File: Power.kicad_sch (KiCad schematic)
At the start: 82 parts, among them Q1 WPM1481-6/TR, U1 H3, U2 AXP223_C2997893

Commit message: linking symbols to footprints
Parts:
- C1, C10, C13, C14, C2, C27, C29, C3, C30, C31, C32, C33, C34, C36, C4, C41, C42, C43, C44, C45, C46, C47, C48, C49, C50, C53, C54, C55, C56, C57, C59, C60, C61, C62, C64, C72, C73, C75, C76, C79, C8, C80, C81, C84, C85, C86, C9: footprint (none) -> Capacitor_SMD:C_0603_1608Metric
- C11, C12, C35, C51, C52, C58, C63, C74, C77, C78, C82, C83: footprint (none) -> Capacitor_SMD:C_0402_1005Metric
- C28, C5, C6, C65, C7, C70, C71: footprint (none) -> Capacitor_SMD:C_0805_2012Metric
- L1, L2, L3, L4, L6, L7: footprint (none) -> Inductor_SMD:L_0402_1005Metric
- R10, R11, R12, R13, R6, R8, R9: footprint (none) -> Resistor_SMD:R_0402_1005Metric
- U1: footprint BGA347_H3_AWT -> (none)

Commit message: placed major components
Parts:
- C1, C10, C13, C14, C2, C27, C29, C3, C30, C31, C32, C33, C34, C36, C4, C41, C42, C43, C44, C45, C46, C47, C48, C49, C50, C53, C54, C55, C56, C57, C59, C60, C61, C62, C64, C72, C73, C75, C76, C79, C8, C80, C81, C84, C85, C86, C9: footprint Capacitor_SMD:C_0603_1608Metric -> Capacitor_SMD:C_0402_1005Metric
- C28, C5, C6, C65, C7: footprint Capacitor_SMD:C_0805_2012Metric -> Capacitor_SMD:C_0402_1005Metric
- C70, C71: footprint Capacitor_SMD:C_0805_2012Metric -> Capacitor_SMD:C_0603_1608Metric
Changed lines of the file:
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@@
 			)
 		)
-		(property "Footprint" "Capacitor_SMD:C_0603_1608Metric"
+		(property "Footprint" "Capacitor_SMD:C_0402_1005Metric"
 			(at 332.74 110.7948 0)
 			(effects
@@
 			)
 		)
-		(property "Footprint" "Capacitor_SMD:C_0805_2012Metric"
+		(property "Footprint" "Capacitor_SMD:C_0402_1005Metric"
 			(at 186.9948 186.69 0)
 			(effects
@@
 			)
 		)
-		(property "Footprint" "Capacitor_SMD:C_0603_1608Metric"
+		(property "Footprint" "Capacitor_SMD:C_0402_1005Metric"
 			(at 507.6952 142.24 0)
 			(effects
@@
 			)
 		)
-		(property "Footprint" "Capacitor_SMD:C_0603_1608Metric"
+		(property "Footprint" "Capacitor_SMD:C_0402_1005Metric"
 			(at 501.3452 345.44 0)
 			(effects
@@
 			)
 		)
-		(property "Footprint" "Capacitor_SMD:C_0603_1608Metric"
+		(property "Footprint" "Capacitor_SMD:C_0402_1005Metric"
 			(at 112.0648 132.08 0)
 			(effects
@@
 			)
 		)
-		(property "Footprint" "Capacitor_SMD:C_0603_1608Metric"
+		(property "Footprint" "Capacitor_SMD:C_0402_1005Metric"
 			(at 325.12 100.0252 0)
 			(effects
@@
 			)
 		)
-		(property "Footprint" "Capacitor_SMD:C_0603_1608Metric"
+		(property "Footprint" "Capacitor_SMD:C_0402_1005Metric"
 			(at 162.8648 331.47 0)
 			(effects
@@
 			)
 		)
-		(property "Footprint" "Capacitor_SMD:C_0805_2012Metric"
+		(property "Footprint" "Capacitor_SMD:C_0402_1005Metric"
 			(at 103.1748 132.08 0)
 			(effects
@@
 			)
 		)
-		(property "Footprint" "Capacitor_SMD:C_0603_1608Metric"
+		(property "Footprint" "Capacitor_SMD:C_0402_1005Metric"
 			(at 487.3752 82.55 0)
 			(effects
@@
 			)
 		)
-		(property "Footprint" "Capacitor_SMD:C_0603_1608Metric"
+		(property "Footprint" "Capacitor_SMD:C_0402_1005Metric"
 			(at 169.2148 331.47 0)
 			(effects
@@
 			)
 		)
-		(property "Footprint" "Capacitor_SMD:C_0603_1608Metric"
+		(property "Footprint" "Capacitor_SMD:C_0402_1005Metric"
 			(at 436.5752 345.44 0)
 			(effects
@@
 			)
 		)
-		(property "Footprint" "Capacitor_SMD:C_0603_1608Metric"
+		(property "Footprint" "Capacitor_SMD:C_0402_1005Metric"
 			(at 190.8048 88.9 0)
 			(effects
@@
 			)
 		)
-		(property "Footprint" "Capacitor_SMD:C_0603_1608Metric"
+		(property "Footprint" "Capacitor_SMD:C_0402_1005Metric"
 			(at 174.2948 186.69 0)
 			(effects
@@
 			)
 		)
-		(property "Footprint" "Capacitor_SMD:C_0603_1608Metric"
+		(property "Footprint" "Capacitor_SMD:C_0402_1005Metric"
 			(at 501.3452 142.24 0)
 			(effects
@@
 			)
 		)
-		(property "Footprint" "Capacitor_SMD:C_0805_2012Metric"
+		(property "Footprint" "Capacitor_SMD:C_0603_1608Metric"
 			(at 442.9252 300.99 0)
 			(effects
@@
 			)
 		)
-		(property "Footprint" "Capacitor_SMD:C_0603_1608Metric"
+		(property "Footprint" "Capacitor_SMD:C_0402_1005Metric"
 			(at 145.0848 293.37 0)
 			(effects
@@
 			)
 		)
-		(property "Footprint" "Capacitor_SMD:C_0603_1608Metric"
+		(property "Footprint" "Capacitor_SMD:C_0402_1005Metric"
 			(at 474.6752 300.99 0)
 			(effects
@@
 			)
 		)
-		(property "Footprint" "Capacitor_SMD:C_0805_2012Metric"
+		(property "Footprint" "Capacitor_SMD:C_0402_1005Metric"
 			(at 184.4548 88.9 0)
 			(effects
@@
 			)
 		)
-		(property "Footprint" "Capacitor_SMD:C_0603_1608Metric"
+		(property "Footprint" "Capacitor_SMD:C_0402_1005Metric"
 			(at 171.7548 129.54 0)
 			(effects
@@
 			)
 		)
-		(property "Footprint" "Capacitor_SMD:C_0603_1608Metric"
+		(property "Footprint" "Capacitor_SMD:C_0402_1005Metric"
 			(at 183.1848 129.54 0)
 			(effects
@@
 			)
 		)
-		(property "Footprint" "Capacitor_SMD:C_0603_1608Metric"
+		(property "Footprint" "Capacitor_SMD:C_0402_1005Metric"
 			(at 184.4548 331.47 0)
 			(effects
@@
 			)
 		)
-		(property "Footprint" "Capacitor_SMD:C_0603_1608Metric"
+		(property "Footprint" "Capacitor_SMD:C_0402_1005Metric"
 			(at 502.6152 82.55 0)
 			(effects
@@
 			)
 		)
-		(property "Footprint" "Capacitor_SMD:C_0603_1608Metric"
+		(property "Footprint" "Capacitor_SMD:C_0402_1005Metric"
 			(at 137.4648 293.37 0)
 			(effects
@@
 			)
 		)
-		(property "Footprint" "Capacitor_SMD:C_0603_1608Metric"
+		(property "Footprint" "Capacitor_SMD:C_0402_1005Metric"
 			(at 171.7548 88.9 0)
 			(effects
@@
 			)
 		)
-		(property "Footprint" "Capacitor_SMD:C_0603_1608Metric"
+		(property "Footprint" "Capacitor_SMD:C_0402_1005Metric"
 			(at 180.6448 186.69 0)
 			(effects
@@
 			)
 		)
-		(property "Footprint" "Capacitor_SMD:C_0603_1608Metric"
+		(property "Footprint" "Capacitor_SMD:C_0402_1005Metric"
 			(at 325.12 82.2452 0)
 			(effects
@@
 			)
 		)
-		(property "Footprint" "Capacitor_SMD:C_0805_2012Metric"
+		(property "Footprint" "Capacitor_SMD:C_0603_1608Metric"
 			(at 436.5752 300.99 0)
 			(effects
@@
 			)
 		)
-		(property "Footprint" "Capacitor_SMD:C_0603_1608Metric"
+		(property "Footprint" "Capacitor_SMD:C_0402_1005Metric"
 			(at 455.6252 345.44 0)
 			(effects
@@
 			)
 		)
-		(property "Footprint" "Capacitor_SMD:C_0603_1608Metric"
+		(property "Footprint" "Capacitor_SMD:C_0402_1005Metric"
 			(at 481.0252 142.24 0)
 			(effects
@@
 			)
 		)
-		(property "Footprint" "Capacitor_SMD:C_0603_1608Metric"
+		(property "Footprint" "Capacitor_SMD:C_0402_1005Metric"
 			(at 152.7048 293.37 0)
 			(effects
@@
 			)
 		)
-		(property "Footprint" "Capacitor_SMD:C_0603_1608Metric"
+		(property "Footprint" "Capacitor_SMD:C_0402_1005Metric"
 			(at 494.9952 82.55 0)
 			(effects
@@
 			)
 		)
-		(property "Footprint" "Capacitor_SMD:C_0603_1608Metric"
+		(property "Footprint" "Capacitor_SMD:C_0402_1005Metric"
 			(at 494.9952 345.44 0)
 			(effects
@@
 			)
 		)
-		(property "Footprint" "Capacitor_SMD:C_0603_1608Metric"
+		(property "Footprint" "Capacitor_SMD:C_0402_1005Metric"
 			(at 461.9752 345.44 0)
 			(effects
@@
 			)
 		)
-		(property "Footprint" "Capacitor_SMD:C_0603_1608Metric"
+		(property "Footprint" "Capacitor_SMD:C_0402_1005Metric"
 			(at 167.9448 293.37 0)
 			(effects
@@
 			)
 		)
-		(property "Footprint" "Capacitor_SMD:C_0603_1608Metric"
+		(property "Footprint" "Capacitor_SMD:C_0402_1005Metric"
 			(at 489.9152 300.99 0)
 			(effects
@@
 			)
 		)
-		(property "Footprint" "Capacitor_SMD:C_0603_1608Metric"
+		(property "Footprint" "Capacitor_SMD:C_0402_1005Metric"
 			(at 382.5748 143.51 0)
 			(effects
@@
 			)
 		)
-		(property "Footprint" "Capacitor_SMD:C_0603_1608Metric"
+		(property "Footprint" "Capacitor_SMD:C_0402_1005Metric"
 			(at 461.9752 300.99 0)
 			(effects
@@
 			)
 		)
-		(property "Footprint" "Capacitor_SMD:C_0603_1608Metric"
+		(property "Footprint" "Capacitor_SMD:C_0402_1005Metric"
 			(at 109.5248 86.36 0)
 			(effects
@@
 			)
 		)
-		(property "Footprint" "Capacitor_SMD:C_0603_1608Metric"
+		(property "Footprint" "Capacitor_SMD:C_0402_1005Metric"
 			(at 494.9952 142.24 0)
 			(effects
@@
 			)
 		)
-		(property "Footprint" "Capacitor_SMD:C_0603_1608Metric"
+		(property "Footprint" "Capacitor_SMD:C_0402_1005Metric"
 			(at 488.6452 142.24 0)
 			(effects
@@
 			)
 		)
-		(property "Footprint" "Capacitor_SMD:C_0603_1608Metric"
+		(property "Footprint" "Capacitor_SMD:C_0402_1005Metric"
 			(at 520.3952 142.24 0)
 			(effects
@@
 			)
 		)
-		(property "Footprint" "Capacitor_SMD:C_0603_1608Metric"
+		(property "Footprint" "Capacitor_SMD:C_0402_1005Metric"
 			(at 43.18 316.5348 0)
 			(effects
@@
 			)
 		)
-		(property "Footprint" "Capacitor_SMD:C_0603_1608Metric"
+		(property "Footprint" "Capacitor_SMD:C_0402_1005Metric"
 			(at 178.1048 88.9 0)
 			(effects
@@
 			)
 		)
-		(property "Footprint" "Capacitor_SMD:C_0603_1608Metric"
+		(property "Footprint" "Capacitor_SMD:C_0402_1005Metric"
 			(at 95.5548 132.08 0)
 			(effects
@@
 			)
 		)
-		(property "Footprint" "Capacitor_SMD:C_0603_1608Metric"
+		(property "Footprint" "Capacitor_SMD:C_0402_1005Metric"
 			(at 515.3152 110.49 0)
 			(effects
@@
 			)
 		)
-		(property "Footprint" "Capacitor_SMD:C_0603_1608Metric"
+		(property "Footprint" "Capacitor_SMD:C_0402_1005Metric"
 			(at 396.5448 87.63 0)
 			(effects
@@
 			)
 		)
-		(property "Footprint" "Capacitor_SMD:C_0603_1608Metric"
+		(property "Footprint" "Capacitor_SMD:C_0402_1005Metric"
 			(at 475.9452 345.44 0)
 			(effects
@@
 			)
 		)
-		(property "Footprint" "Capacitor_SMD:C_0603_1608Metric"
+		(property "Footprint" "Capacitor_SMD:C_0402_1005Metric"
 			(at 449.2752 300.99 0)
 			(effects
@@
 			)
 		)
-		(property "Footprint" "Capacitor_SMD:C_0603_1608Metric"
+		(property "Footprint" "Capacitor_SMD:C_0402_1005Metric"
 			(at 193.3448 186.69 0)
 			(effects
@@
 			)
 		)
-		(property "Footprint" "Capacitor_SMD:C_0805_2012Metric"
+		(property "Footprint" "Capacitor_SMD:C_0402_1005Metric"
 			(at 100.6348 86.36 0)
 			(effects
@@
 			)
 		)
-		(property "Footprint" "Capacitor_SMD:C_0603_1608Metric"
+		(property "Footprint" "Capacitor_SMD:C_0402_1005Metric"
 			(at 473.4052 142.24 0)
 			(effects
@@
 			)
 		)
-		(property "Footprint" "Capacitor_SMD:C_0805_2012Metric"
+		(property "Footprint" "Capacitor_SMD:C_0402_1005Metric"
 			(at 189.5348 129.54 0)
 			(effects
@@
 			)
 		)
-		(property "Footprint" "Capacitor_SMD:C_0603_1608Metric"
+		(property "Footprint" "Capacitor_SMD:C_0402_1005Metric"
 			(at 93.0148 86.36 0)
 			(effects
@@
 			)
 		)
-		(property "Footprint" "Capacitor_SMD:C_0603_1608Metric"
+		(property "Footprint" "Capacitor_SMD:C_0402_1005Metric"
 			(at 175.5648 293.37 0)
 			(effects

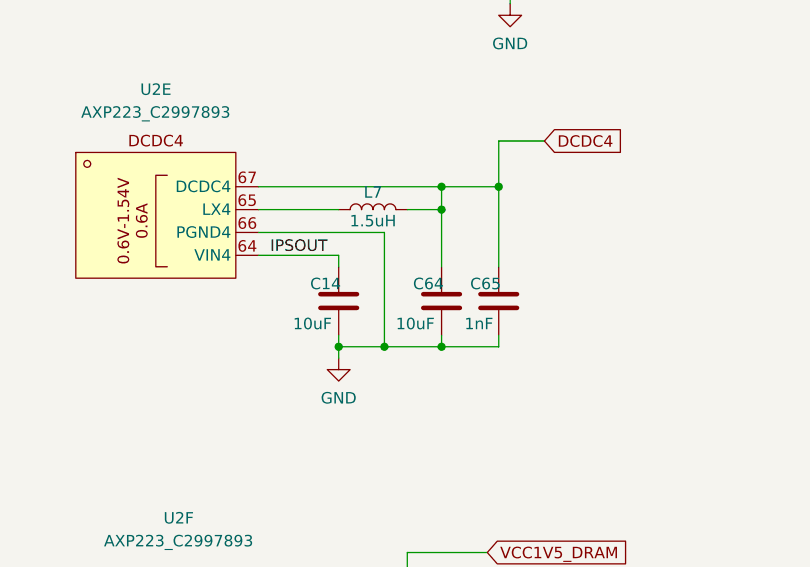
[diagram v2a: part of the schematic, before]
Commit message: placing capacitors
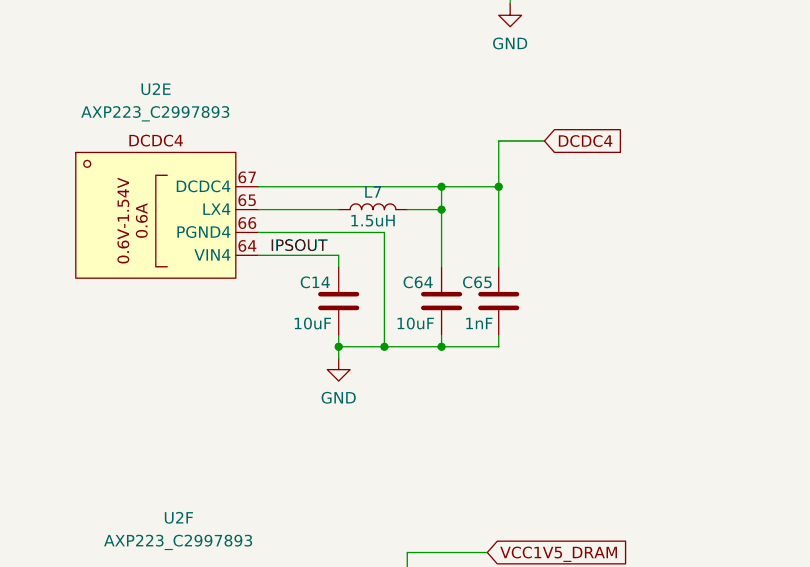
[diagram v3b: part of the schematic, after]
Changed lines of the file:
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@@
 		(dnp no)
 		(property "Reference" "C14"
-			(at 169.545 131.445 0)
+			(at 168.402 131.318 0)
 			(effects
 				(font
@@
 		(dnp no)
 		(property "Reference" "C64"
-			(at 180.975 131.445 0)
+			(at 179.832 131.318 0)
 			(effects
 				(font
@@
 		(dnp no)
 		(property "Reference" "C65"
-			(at 187.325 131.445 0)
+			(at 186.436 131.318 0)
 			(effects
 				(font

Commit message: started RAM routing, might move to 1 module though
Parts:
- U1: footprint (none) -> easyeda2kicad:BGA-347_L14.0-W14.0-R21-C21-P0.65-TL
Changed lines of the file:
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@@
 			)
 		)
-		(property "Footprint" ""
+		(property "Footprint" "easyeda2kicad:BGA-347_L14.0-W14.0-R21-C21-P0.65-TL"
 			(at 284.48 267.97 0)
 			(effects
@@
 			)
 		)
-		(property "Footprint" ""
+		(property "Footprint" "easyeda2kicad:BGA-347_L14.0-W14.0-R21-C21-P0.65-TL"
 			(at 195.58 261.62 0)
 			(effects
@@
 			)
 		)
-		(property "Footprint" ""
+		(property "Footprint" "easyeda2kicad:BGA-347_L14.0-W14.0-R21-C21-P0.65-TL"
 			(at 64.77 248.92 0)
 			(effects

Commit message: placed all decaps, emmc routing changes, DDR routing changes
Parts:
- removed C72: 10uF, Capacitor_SMD:C_0402_1005Metric, symbol Device:C
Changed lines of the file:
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@@
 	)
 	(junction
-		(at 441.96 303.53)
-		(diameter 0)
-		(color 0 0 0 0)
-	)
-	(junction
 		(at 506.73 129.54)
 		(diameter 0)
@@
 	)
 	(junction
-		(at 441.96 290.83)
-		(diameter 0)
-		(color 0 0 0 0)
-	)
-	(junction
 		(at 279.4 280.67)
 		(diameter 0)
@@
 	(wire
 		(pts
-			(xy 448.31 293.37) (xy 448.31 290.83)
-		)
-		(stroke
-			(width 0)
-			(type default)
-		)
-	)
-	(wire
-		(pts
 			(xy 279.4 280.67) (xy 284.48 280.67)
 		)
@@
 	(wire
 		(pts
-			(xy 448.31 303.53) (xy 441.96 303.53)
-		)
-		(stroke
-			(width 0)
-			(type default)
-		)
-	)
-	(wire
-		(pts
 			(xy 298.45 88.9) (xy 298.45 93.98)
 		)
@@
 	(wire
 		(pts
-			(xy 448.31 290.83) (xy 441.96 290.83)
-		)
-		(stroke
-			(width 0)
-			(type default)
-		)
-	)
-	(wire
-		(pts
 			(xy 59.69 304.8) (xy 59.69 307.34)
 		)
@@
 	(wire
 		(pts
-			(xy 448.31 300.99) (xy 448.31 303.53)
-		)
-		(stroke
-			(width 0)
-			(type default)
-		)
-	)
-	(wire
-		(pts
 			(xy 421.64 91.44) (xy 416.56 91.44)
 		)
@@
 					(unit 1)
 				)
-			)
-		)
-	)
-	(symbol
-		(lib_id "Device:C")
-		(at 448.31 297.18 0)
-		(unit 1)
-		(exclude_from_sim no)
-		(in_bom yes)
-		(on_board yes)
-		(dnp no)
-		(property "Reference" "C72"
-			(at 449.072 294.894 0)
-			(effects
-				(font
-					(size 1.27 1.27)
-				)
-				(justify left)
-			)
-		)
-		(property "Value" "10uF"
-			(at 449.072 299.974 0)
-			(effects
-				(font
-					(size 1.27 1.27)
-				)
-				(justify left)
-			)
-		)
-		(property "Footprint" "Capacitor_SMD:C_0402_1005Metric"
-			(at 449.2752 300.99 0)
-			(effects
-				(font
-					(size 1.27 1.27)
-				)
-				(hide yes)
-			)
-		)
-		(property "Datasheet" "~"
-			(at 448.31 297.18 0)
-			(effects
-				(font
-					(size 1.27 1.27)
-				)
-				(hide yes)
-			)
-		)
-		(property "Description" "Unpolarized capacitor"
-			(at 448.31 297.18 0)
-			(effects
-				(font
-					(size 1.27 1.27)
-				)
-				(hide yes)
-			)
-		)
-		(pin "1"
-		)
-		(pin "2"
-		)
-		(instances
-			(project "H3_SBC"
-				(path "/2511caf5-b791-49bc-bcf7-734707cf883b/83d14ca4-74e6-4527-889a-72c0efdaf06d"
-					(reference "C72")
-					(unit 1)
-				)
